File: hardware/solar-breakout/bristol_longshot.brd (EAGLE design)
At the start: 65 parts, among them U1 SPV1040, U2 SPV1040, U3 LT4054ES5-4.2, U4 TPS62243, U5 TPS62243, U6 TPS3808, U7 74LVC1G04GW

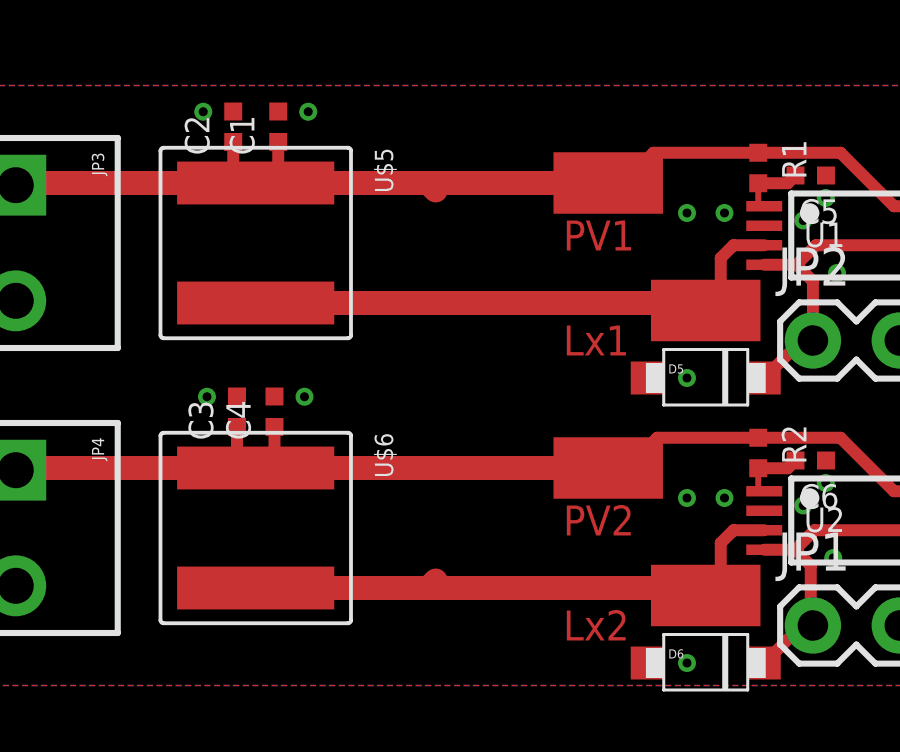
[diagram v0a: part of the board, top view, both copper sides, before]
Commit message: Added LPS3015 mppt inductor footprint alongside XAL6060 footprint
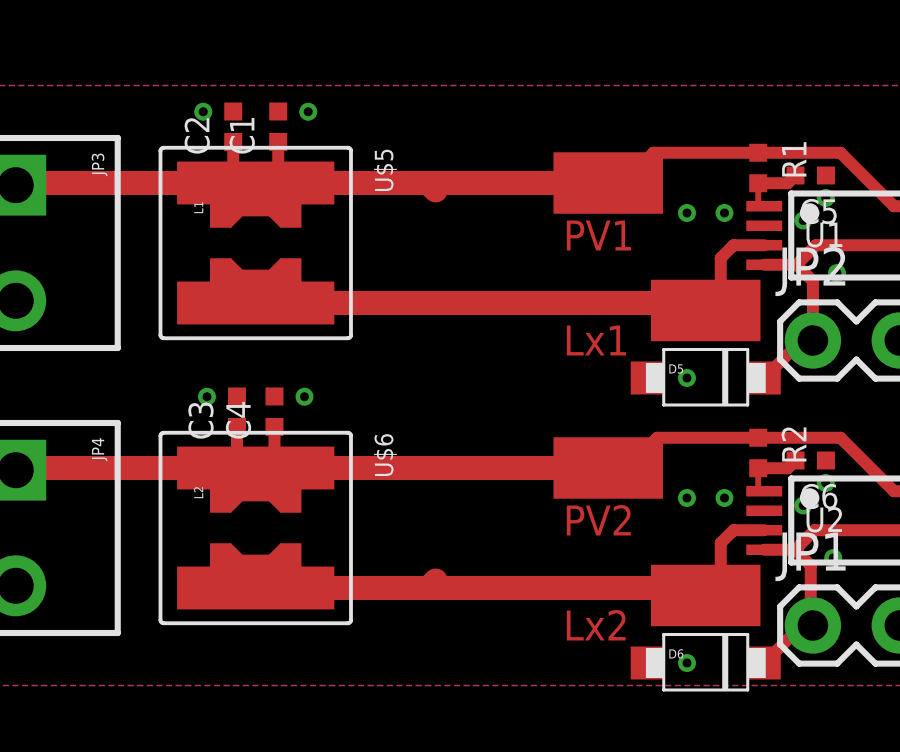
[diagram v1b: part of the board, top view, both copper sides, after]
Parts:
- added L1, L2: 10uH LPS3015, PecanFemto4:LPS3015
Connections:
- net LX1: now also L1.2_1, L1.2_2, L1.2_3, L1.2_4, L1.2_5, L1.2_6, L1.2_7, L1.2_8, L1.2_9
- net LX2: now also L2.2_1, L2.2_2, L2.2_3, L2.2_4, L2.2_5, L2.2_6, L2.2_7, L2.2_8, L2.2_9
- net PV1: now also L1.1_1, L1.1_2, L1.1_3, L1.1_4, L1.1_5, L1.1_6, L1.1_7, L1.1_8, L1.1_9
- net PV2: now also L2.1_1, L2.1_2, L2.1_3, L2.1_4, L2.1_5, L2.1_6, L2.1_7, L2.1_8, L2.1_9
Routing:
- net PV1: track 36.3 -> 41.8 mm
- net LX1: track 18.7 -> 24.1 mm
- net LX2: track 19.0 -> 24.2 mm
- net PV2: track 35.5 -> 40.7 mm
